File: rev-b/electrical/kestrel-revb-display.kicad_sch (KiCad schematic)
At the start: 36 parts, among them J1001 LCD RGB / contact fit pending, J1002 CAP TOUCH / contact fit pendi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

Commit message: Place sixteen RGB source damping resistors on the underside
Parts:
- R1001, R1002, R1003, R1004, R1005, R1006, R1007, R1008, R1009, R1010, R1011, R1012, R1013, R1014, R1015, R1016: AssemblySide (none) -> B.Cu / source damping passives; assembly qualification pend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
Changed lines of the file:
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@@
+			)
+		)
+		(property "AssemblySide" "B.Cu / source damping passives; assembly qualification pending"
+			(at 35.56 185.42000000000002 0)
+			(effects
+				(font
+					(size 1 1)
+				)
+				(hide yes)
 			)
 		)
@@
 			)
 		)
+		(property "AssemblySide" "B.Cu / source damping passives; assembly qualification pending"
+			(at 124.46000000000001 185.42000000000002 0)
+			(effects
+				(font
+					(size 1 1)
+				)
+				(hide yes)
+			)
+		)
 	)
 	(symbol
@@
 			)
 		)
+		(property "AssemblySide" "B.Cu / source damping passives; assembly qualification pending"
+			(at 214.63 185.42000000000002 0)
+			(effects
+				(font
+					(size 1 1)
+				)
+				(hide yes)
+			)
+		)
 	)
 	(symbol
@@
 			)
 		)
+		(property "AssemblySide" "B.Cu / source damping passives; assembly qualification pending"
+			(at 304.8 185.42000000000002 0)
+			(effects
+				(font
+					(size 1 1)
+				)
+				(hide yes)
+			)
+		)
 	)
 	(symbol
@@
 			)
 		)
+		(property "AssemblySide" "B.Cu / source damping passives; assembly qualification pending"
+			(at 394.97 185.42000000000002 0)
+			(effects
+				(font
+					(size 1 1)
+				)
+				(hide yes)
+			)
+		)
 	)
 	(symbol
@@
 			)
 		)
+		(property "AssemblySide" "B.Cu / source damping passives; assembly qualification pending"
+			(at 485.14 185.42000000000002 0)
+			(effects
+				(font
+					(size 1 1)
+				)
+				(hide yes)
+			)
+		)
 	)
 	(symbol
@@
 			)
 		)
+		(property "AssemblySide" "B.Cu / source damping passives; assembly qualification pending"
+			(at 35.56 224.79 0)
+			(effects
+				(font
+					(size 1 1)
+				)
+				(hide yes)
+			)
+		)
 	)
 	(symbol
@@
 			)
 		)
+		(property "AssemblySide" "B.Cu / source damping passives; assembly qualification pending"
+			(at 124.46000000000001 224.79 0)
+			(effects
+				(font
+					(size 1 1)
+				)
+				(hide yes)
+			)
+		)
 	)
 	(symbol
@@
 			)
 		)
+		(property "AssemblySide" "B.Cu / source damping passives; assembly qualification pending"
+			(at 214.63 224.79 0)
+			(effects
+				(font
+					(size 1 1)
+				)
+				(hide yes)
+			)
+		)
 	)
 	(symbol
@@
 			)
 		)
+		(property "AssemblySide" "B.Cu / source damping passives; assembly qualification pending"
+			(at 304.8 224.79 0)
+			(effects
+				(font
+					(size 1 1)
+				)
+				(hide yes)
+			)
+		)
 	)
 	(symbol
@@
 			)
 		)
+		(property "AssemblySide" "B.Cu / source damping passives; assembly qualification pending"
+			(at 394.97 224.79 0)
+			(effects
+				(font
+					(size 1 1)
+				)
+				(hide yes)
+			)
+		)
 	)
 	(symbol
@@
 			)
 		)
+		(property "AssemblySide" "B.Cu / source damping passives; assembly qualification pending"
+			(at 485.14 224.79 0)
+			(effects
+				(font
+					(size 1 1)
+				)
+				(hide yes)
+			)
+		)
 	)
 	(symbol
@@
 			)
 		)
+		(property "AssemblySide" "B.Cu / source damping passives; assembly qualification pending"
+			(at 35.56 265.43 0)
+			(effects
+				(font
+					(size 1 1)
+				)
+				(hide yes)
+			)
+		)
 	)
 	(symbol
@@
 			)
 		)
+		(property "AssemblySide" "B.Cu / source damping passives; assembly qualification pending"
+			(at 124.46000000000001 265.43 0)
+			(effects
+				(font
+					(size 1 1)
+				)
+				(hide yes)
+			)
+		)
 	)
 	(symbol
@@
 			)
 		)
+		(property "AssemblySide" "B.Cu / source damping passives; assembly qualification pending"
+			(at 214.63 265.43 0)
+			(effects
+				(font
+					(size 1 1)
+				)
+				(hide yes)
+			)
+		)
 	)
 	(symbol
@@
 			(at 304.8 265.43 0)
 			(effects
+				(font
+					(size 1 1)
+				)
+				(hide yes)
+			)
+		)
+		(property "AssemblySide" "B.Cu / source damping passives; assembly qualification pending"
+			(at 304.8 265.43 0)
+			(effects

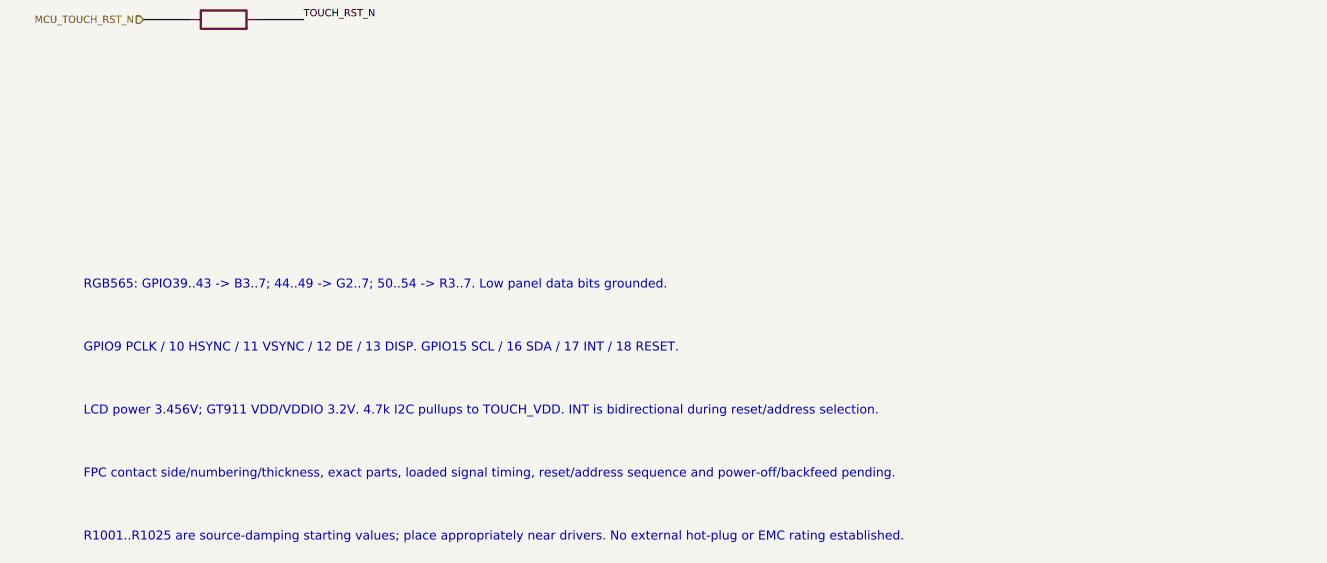
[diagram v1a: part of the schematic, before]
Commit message: Route all sixteen RGB source signals with guarded via-in-pad
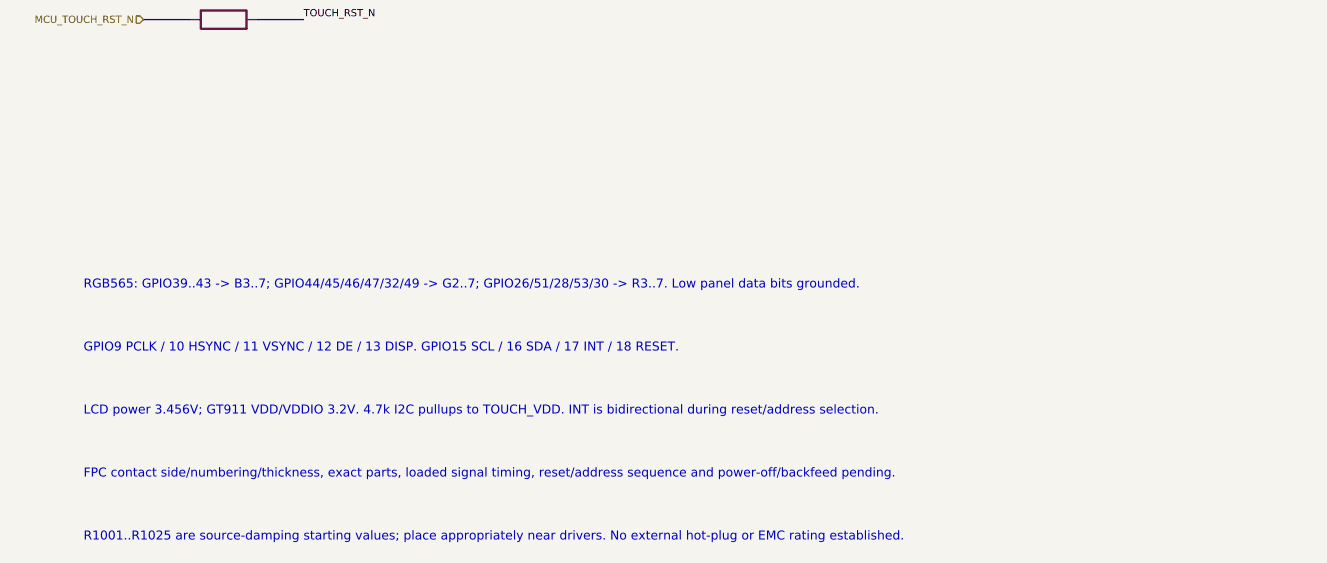
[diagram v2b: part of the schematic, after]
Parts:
- R1001, R1002, R1003, R1004, R1005, R1006, R1007, R1008, R1009, R1010, R1011, R1012, R1013, R1014, R1015, R1016: footprint Resistor_SMD:R_0603_1608Metric -> Resistor_SMD:R_0402_1005Metric; LCSC (none) -> C138002; MPN (none) -> RC0402FR-0733RL; Manufacturer (none) -> YAGEO; Rating 33ohm / 1% / GPIO source damping starting value -> 33ohm / 1% / 0.063W at 70C / 50V limiting voltage / GPIO so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
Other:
- note added: "RGB565: GPIO39..43 -> B3..7; GPIO44/45/46/47/32/49 -> G2..7; GPIO26/51/28/53/30 -> R3..7. Low panel data bits grounded."
- note removed: "RGB565: GPIO39..43 -> B3..7; 44..49 -> G2..7; 50..54 -> R3..7. Low panel data bits grounded."

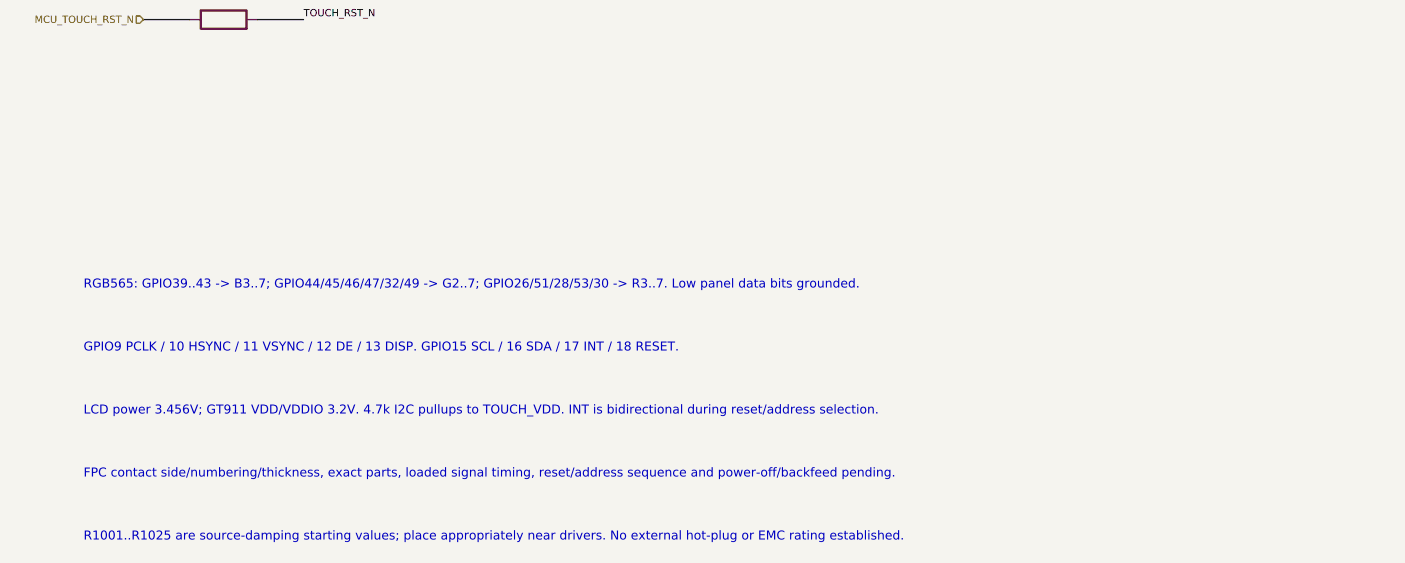
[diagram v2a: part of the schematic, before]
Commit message: Complete all sixteen RGB resistor-to-FPC routes
Coordinate R4/R6 source GPIOs and underside poses with guarded source replacement. Add independently checked output topology, native clearance and preservation evidence, and current schematic/PCB review artifacts.
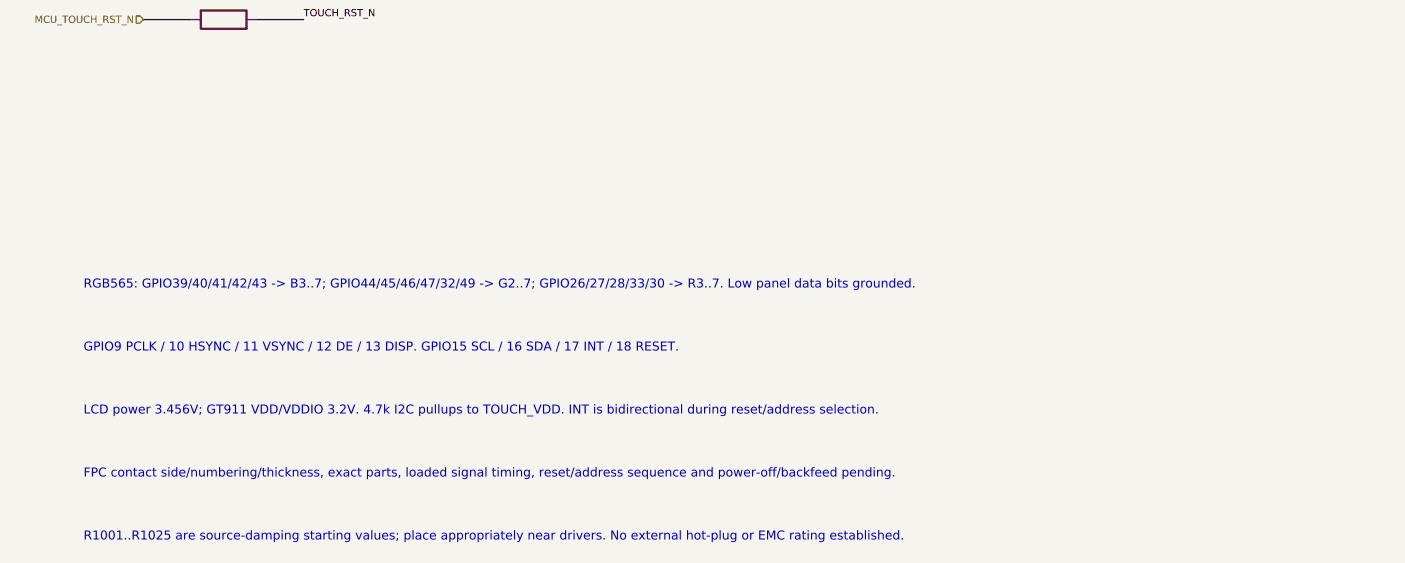
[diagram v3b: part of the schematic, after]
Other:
- note added: "RGB565: GPIO39/40/41/42/43 -> B3..7; GPIO44/45/46/47/32/49 -> G2..7; GPIO26/27/28/33/30 -> R3..7. Low panel data bits grounded."
- note removed: "RGB565: GPIO39..43 -> B3..7; GPIO44/45/46/47/32/49 -> G2..7; GPIO26/51/28/53/30 -> R3..7. Low panel data bits grounded."
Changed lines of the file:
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@@
 		)
 	)
-	(text "RGB565: GPIO39..43 -> B3..7; GPIO44/45/46/47/32/49 -> G2..7; GPIO26/51/28/53/30 -> R3..7. Low panel data bits grounded."
+	(text "RGB565: GPIO39/40/41/42/43 -> B3..7; GPIO44/45/46/47/32/49 -> G2..7; GPIO26/27/28/33/30 -> R3..7. Low panel data bits grounded."
 		(at 20 375 0)
 		(effects
